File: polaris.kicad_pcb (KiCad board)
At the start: 4 copper layers, 75 x 155 mm, 163 parts, among them J1001 Conn_Coaxial, J101 XT60-M, J102 PYRO0, J103 PYRO1, J104 PYRO2, J105 PYRO3, J106 PYRO4, J107 PYRO5, J108 SERVO0, J109 SERVO1, J110 SERVO2, J111 SERVO3, J112 SERVO4, J113 SERVO5, J114 SPI, J115 I2C, J116 PB, J117 SWD, J301 USB_C_Receptacle_USB2.0_16P, J401 GNSS, J501 XT60-M, Q201 IRLZ44N, Q202 IRLZ44N, Q401 Q_NMOS, Q501 IRLZ44N, Q502 IRLZ44N, Q503 IRLZ44N, Q504 IRLZ44N, Q505 IRLZ44N, Q506 IRLZ44N, SW401 SW_Push, SW402 SW_Push, U1001 Ra-08H, U1101 THD-2528-11SD-GF, U1201 W25Q128JVE, U201 BQ24005, U202 LM74700, U203 LM74700, U204 TLV75733PDBV, U205 LMR51430, U206 TPS7A2033PDBVR, U301 USBLC6-2SC6, U302 CH224K, U303 USBLC6-2SC6, U403 STM32F446VETx, U501 PC817, U502 PC817, U503 PC817, U504 PC817, U505 PC817, U506 PC817, U507 CD4051B, U601 ICM-42688-P, U701 LSM6DSO32TR, U801 MS5607, U901 LPS22HH, Y401 YXC YSX321SL

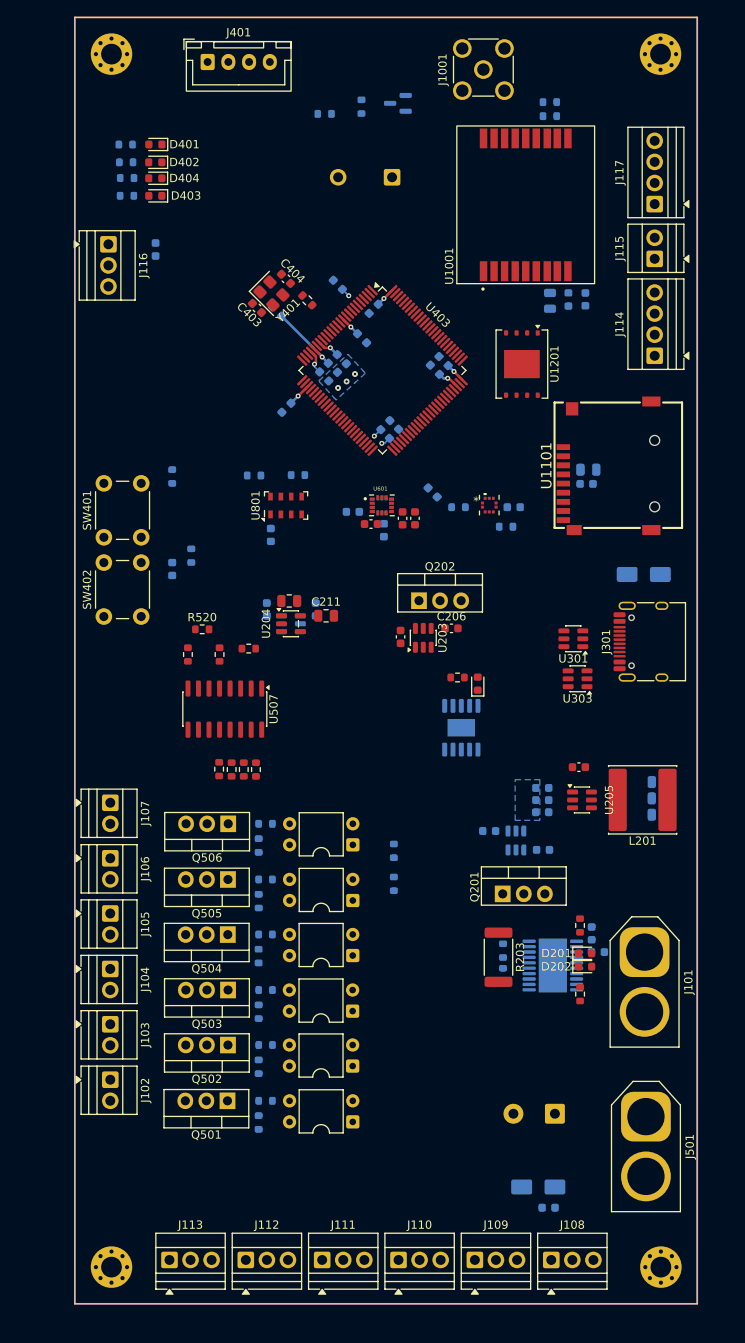
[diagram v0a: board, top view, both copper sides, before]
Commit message: Re-annotated schematic
Continued laying out traces on PCB
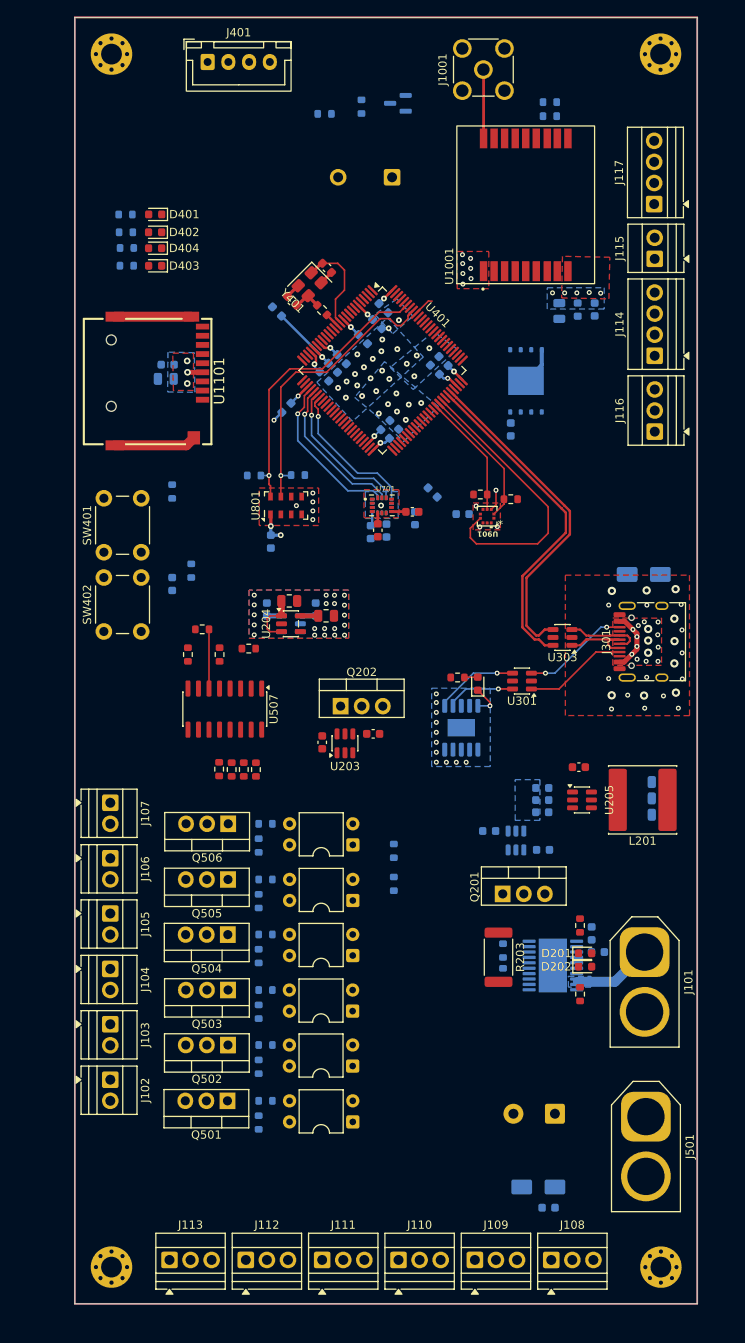
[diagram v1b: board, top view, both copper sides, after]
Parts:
- C601, C602, C603, U1201, U601: moved to B.Cu
- C701, C702, R901, R902, U701: moved to F.Cu
- moved J116 69.6 mm to (156.9, 74.9), turned to 90 degrees
- moved U1101 55.0 mm to (97.1, 68.8), turned to -90 degrees
- moved C1102 52.5 mm to (98.2, 66.8), turned to 180 degrees
- moved C1101 52.1 mm to (98.0, 68.6), turned to 180 degrees
- moved C1201 48.0 mm to (139.5, 74.6), turned to -90 degrees
- moved U203 15.8 mm to (119.5, 112.5)
- moved C206 15.8 mm to (123.0, 111.3)
- moved C204 15.8 mm to (116.8, 112.3)
- moved Q202 15.8 mm to (119.0, 108.0)
- moved C403 9.72 mm to (117.4, 55.2)
- moved D401 8.43 mm to (96.7, 48.7)
- moved D402 8.43 mm to (96.7, 50.9)
- moved D403 8.43 mm to (96.7, 54.9)
- moved D404 8.43 mm to (96.7, 52.8)
- moved R408 8.43 mm to (93.1, 48.7)
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- renumbered U403 to U401
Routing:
- net /2_USB/USB_D-: track 0.00 -> 40.6 mm
- net /2_USB/USB_D+: track 0.00 -> 40.2 mm
- net /3_NavigationProcessor/MS_SDA: track 0.00 -> 35.1 mm, vias 0 -> 1
- net /3_NavigationProcessor/MS_SCL: track 0.00 -> 34.8 mm, vias 0 -> 1
- net /3_NavigationProcessor/LPS_INT: track 0.00 -> 34.3 mm
- net GND: track 0.00 -> 31.3 mm, vias 3 -> 100
- net /3_NavigationProcessor/ICM_CS: track 0.00 -> 19.5 mm, vias 0 -> 1
- net /3_NavigationProcessor/ICM_SCK: track 0.00 -> 18.8 mm, vias 0 -> 1
- net /3_NavigationProcessor/ICM_MOSI: track 0.00 -> 17.8 mm, vias 0 -> 1
- net /3_NavigationProcessor/ICM_MISO: track 0.00 -> 17.7 mm, vias 0 -> 1
- net /3_NavigationProcessor/LPS_SCL: track 0.00 -> 17.0 mm
- net +3.3V: track 27.6 -> 43.0 mm, vias 9 -> 14
- net /3_NavigationProcessor/LPS_SDA: track 0.00 -> 14.9 mm
- net /2_USB/USBC_CC2: track 0.00 -> 12.9 mm, vias 0 -> 2
- net /2_USB/USBC_CC1: track 0.00 -> 12.5 mm
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- added copper zone on B.Cu, net +3.3V
- added copper zone on F.Cu, net +3.3V
- added copper zone on B.Cu, net +3.3VA
- added copper zone on F.Cu, net +3.3VA
- added copper zone on F.Cu, net /1_Power/USB_VCC
- added copper zone on F.Cu, net GND
- added copper zone on B.Cu, net VBAT_VIN
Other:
- board text added: "U901"

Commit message: Continued laying traces
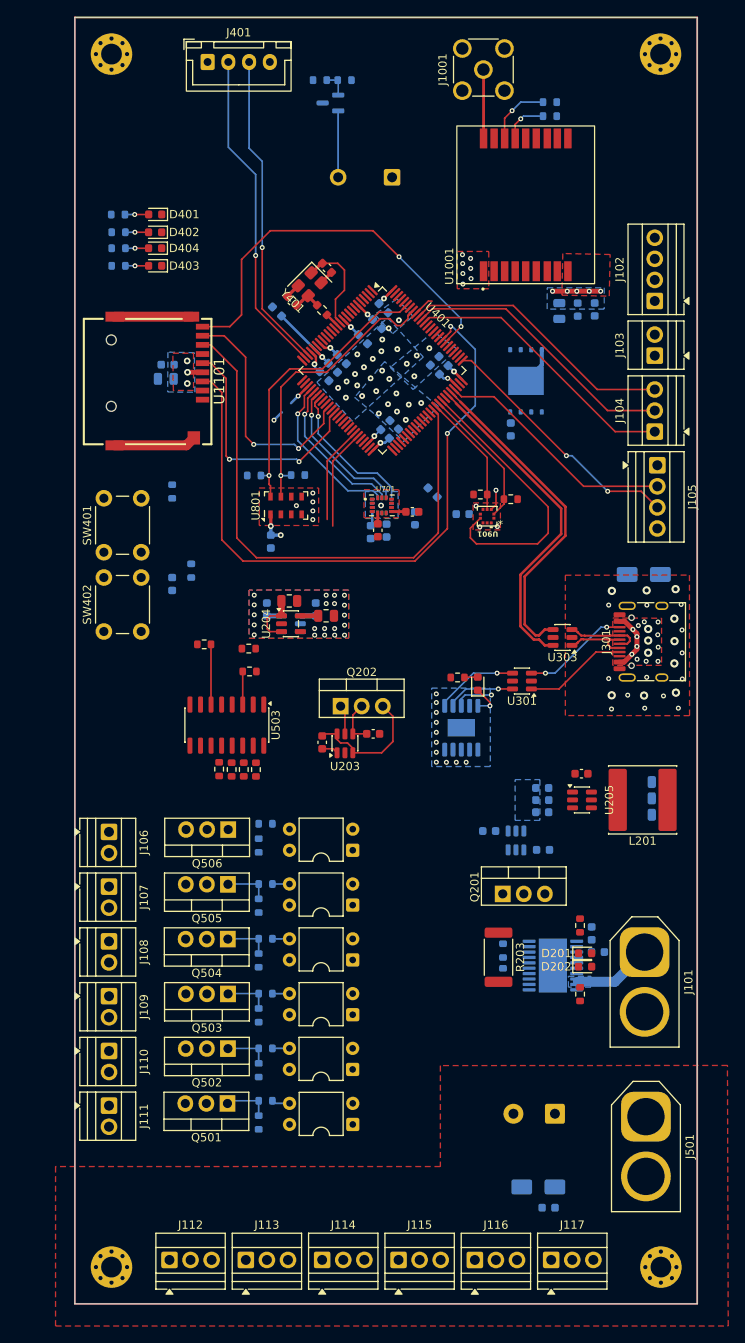
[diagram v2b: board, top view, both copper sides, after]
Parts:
- removed C417, C418, C419: 100n, Capacitor_SMD:C_0603_1608Metric
- removed R412, R413: 180R, Resistor_SMD:R_0603_1608Metric
- removed R414: 47R, Resistor_SMD:R_0603_1608Metric
- removed R415: 47k, Resistor_SMD:R_0603_1608Metric
- removed the R517 at (100.6, 101.8)
- removed the R518 at (104.4, 101.8)
- added C409: 100n, Capacitor_SMD:C_0603_1608Metric, B.Cu at (125.4, 75.2)
- added C412: 100n, Capacitor_SMD:C_0603_1608Metric, B.Cu at (117.1, 68.2)
- added R406: 47R, Resistor_SMD:R_0603_1608Metric, B.Cu at (119.5, 32.6)
- added R407: 47k, Resistor_SMD:R_0603_1608Metric, B.Cu at (116.5, 32.6)
- added R408: 180R, Resistor_SMD:R_0603_1608Metric, B.Cu at (92.3, 54.9)
- added R409: 180R, Resistor_SMD:R_0603_1608Metric, B.Cu at (92.3, 52.8)
- added R508: 1k, Resistor_SMD:R_0603_1608Metric, F.Cu at (108.1, 103.8)
- C406: renamed from C408; value 2u2 -> 4u7
- C410: value 4u7 -> 100n
- J102: value PYRO0 -> SPI; footprint TerminalBlock:TerminalBlock_Xinya_XY308-2.54-2P_1x02_P2.54mm_Horizontal -> TerminalBlock:TerminalBlock_Xinya_XY308-2.54-4P_1x04_P2.54mm_Horizontal
- J103: value PYRO1 -> I2C
- J104: value PYRO2 -> PB; footprint TerminalBlock:TerminalBlock_Xinya_XY308-2.54-2P_1x02_P2.54mm_Horizontal -> TerminalBlock:TerminalBlock_Xinya_XY308-2.54-3P_1x03_P2.54mm_Horizontal
- J105: value PYRO3 -> SWD; footprint TerminalBlock:TerminalBlock_Xinya_XY308-2.54-2P_1x02_P2.54mm_Horizontal -> TerminalBlock:TerminalBlock_Xinya_XY308-2.54-4P_1x04_P2.54mm_Horizontal
- J106: value PYRO4 -> PYRO5
- J107: value PYRO5 -> PYRO4
- J108: value SERVO0 -> PYRO3; footprint TerminalBlock:TerminalBlock_Xinya_XY308-2.54-3P_1x03_P2.54mm_Horizontal -> TerminalBlock:TerminalBlock_Xinya_XY308-2.54-2P_1x02_P2.54mm_Horizontal
- J109: value SERVO1 -> PYRO2; footprint TerminalBlock:TerminalBlock_Xinya_XY308-2.54-3P_1x03_P2.54mm_Horizontal -> TerminalBlock:TerminalBlock_Xinya_XY308-2.54-2P_1x02_P2.54mm_Horizontal
- J110: value SERVO2 -> PYRO1; footprint TerminalBlock:TerminalBlock_Xinya_XY308-2.54-3P_1x03_P2.54mm_Horizontal -> TerminalBlock:TerminalBlock_Xinya_XY308-2.54-2P_1x02_P2.54mm_Horizontal
- J111: value SERVO3 -> PYRO0; footprint TerminalBlock:TerminalBlock_Xinya_XY308-2.54-3P_1x03_P2.54mm_Horizontal -> TerminalBlock:TerminalBlock_Xinya_XY308-2.54-2P_1x02_P2.54mm_Horizontal
- J112: renamed from J113; value SERVO5 -> SERVO0
- J113: renamed from J112; value SERVO4 -> SERVO1
- J114: value SPI -> SERVO2; footprint TerminalBlock:TerminalBlock_Xinya_XY308-2.54-4P_1x04_P2.54mm_Horizontal -> TerminalBlock:TerminalBlock_Xinya_XY308-2.54-3P_1x03_P2.54mm_Horizontal
- J115: value I2C -> SERVO3; footprint TerminalBlock:TerminalBlock_Xinya_XY308-2.54-2P_1x02_P2.54mm_Horizontal -> TerminalBlock:TerminalBlock_Xinya_XY308-2.54-3P_1x03_P2.54mm_Horizontal
- J116: value PB -> SERVO4
- J117: value SWD -> SERVO5; footprint TerminalBlock:TerminalBlock_Xinya_XY308-2.54-4P_1x04_P2.54mm_Horizontal -> TerminalBlock:TerminalBlock_Xinya_XY308-2.54-3P_1x03_P2.54mm_Horizontal
- R517: renamed from R515; value 4k7 -> 47R
- R518: renamed from R516; value 4k7 -> 47R
- R519: value 1k -> 4k7
- U503: value PC817 -> CD4051B; footprint Package_DIP:DIP-4_W7.62mm -> Package_SO:SOIC-16_3.9x9.9mm_P1.27mm
- U507: value CD4051B -> PC817; footprint Package_SO:SOIC-16_3.9x9.9mm_P1.27mm -> Package_DIP:DIP-4_W7.62mm
- moved J117 127.8 mm to (144.4, 174.7), turned to 0 degrees
- moved J115 124.5 mm to (126.0, 174.7), turned to 0 degrees
- moved J114 116.1 mm to (116.8, 174.7), turned to 0 degrees
- moved J102 114.5 mm to (156.9, 59.2), turned to 90 degrees
- moved J103 103.9 mm to (156.9, 65.8), turned to 90 degrees
- moved J116 102.1 mm to (135.2, 174.7), turned to 0 degrees
- moved J104 92.2 mm to (156.9, 74.9), turned to 90 degrees
- moved J105 85.2 mm to (157.2, 79.0)
- moved J108 65.7 mm to (91.1, 136.3), turned to -90 degrees
- moved J109 54.3 mm to (91.1, 142.9), turned to -90 degrees
- moved J110 43.0 mm to (91.1, 149.5), turned to -90 degrees
- moved U503 37.6 mm to (105.3, 110.3), turned to -90 degrees
- moved J111 31.7 mm to (91.1, 156.1), turned to -90 degrees
- moved R207 28.2 mm to (152.4, 116.9)
- moved R206 28.2 mm to (152.4, 121.1)
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- renumbered C403 to C401, C404 to C402, C405 to C403, C406 to C404, C407 to C405, C409 to C407, R405 to R401, R406 to R402, R407 to R403, R408 to R404, R409 to R405, R520 to R507, R507 to R509, R508 to R510, R509 to R511, R510 to R512, R511 to R513, R512 to R514, R513 to R515, R514 to R516
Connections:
- C406 pad 1: Net-(U403-VCAP_1) -> +3.3V
- J102 pad 1: POWER -> /3_NavigationProcessor/SPI4_SCK
- J102 pad 2: /4_Pyrochannels/PYRO_0 -> /3_NavigationProcessor/SPI4_NSS
- J103 pad 1: POWER -> /3_NavigationProcessor/I2C2_SCL
- J103 pad 2: /4_Pyrochannels/PYRO_1 -> /3_NavigationProcessor/I2C2_SDA
- J104 pad 1: POWER -> /3_NavigationProcessor/PB3
- J104 pad 2: /4_Pyrochannels/PYRO_2 -> /3_NavigationProcessor/PB4
- J105 pad 1: POWER -> +3.3V
- J105 pad 2: /4_Pyrochannels/PYRO_3 -> /3_NavigationProcessor/SYS_SWDIO
- J106 pad 2: /4_Pyrochannels/PYRO_4 -> /4_Pyrochannels/PYRO_5
- J107 pad 2: /4_Pyrochannels/PYRO_5 -> /4_Pyrochannels/PYRO_4
- J108 pad 1: /3_NavigationProcessor/SERVO_S0 -> POWER
- J108 pad 2: /4_Pyrochannels/SERVO_PWR -> /4_Pyrochannels/PYRO_3
- J109 pad 1: /3_NavigationProcessor/SERVO_S1 -> POWER
- J109 pad 2: /4_Pyrochannels/SERVO_PWR -> /4_Pyrochannels/PYRO_2
- J110 pad 1: /3_NavigationProcessor/SERVO_S2 -> POWER
- J110 pad 2: /4_Pyrochannels/SERVO_PWR -> /4_Pyrochannels/PYRO_1
- J111 pad 1: /3_NavigationProcessor/SERVO_S3 -> POWER
- J111 pad 2: /4_Pyrochannels/SERVO_PWR -> /4_Pyrochannels/PYRO_0
- J112 pad 1: /3_NavigationProcessor/SERVO_S5 -> /3_NavigationProcessor/SERVO_S0
- J113 pad 1: /3_NavigationProcessor/SERVO_S4 -> /3_NavigationProcessor/SERVO_S1
- J114 pad 1: /3_NavigationProcessor/SPI4_SCK -> /3_NavigationProcessor/SERVO_S2
- J114 pad 2: /3_NavigationProcessor/SPI4_NSS -> /4_Pyrochannels/SERVO_PWR
- J114 pad 3: /3_NavigationProcessor/SPI4_MISO -> GND
- J115 pad 1: /3_NavigationProcessor/I2C2_SCL -> /3_NavigationProcessor/SERVO_S3
- J115 pad 2: /3_NavigationProcessor/I2C2_SDA -> /4_Pyrochannels/SERVO_PWR
- J116 pad 1: /3_NavigationProcessor/PB3 -> /3_NavigationProcessor/SERVO_S4
- J116 pad 2: /3_NavigationProcessor/PB4 -> /4_Pyrochannels/SERVO_PWR
- J116 pad 3: /3_NavigationProcessor/PB5 -> GND
- J117 pad 1: +3.3V -> /3_NavigationProcessor/SERVO_S5
- J117 pad 2: /3_NavigationProcessor/SYS_SWDIO -> /4_Pyrochannels/SERVO_PWR
- J117 pad 3: /3_NavigationProcessor/SYS_SWCLK -> GND
- Q501 pad 2: GND -> /4_Pyrochannels/PYRO_0
- Q501 pad 3: /4_Pyrochannels/PYRO_0 -> GND
- Q502 pad 2: GND -> /4_Pyrochannels/PYRO_1
- Q502 pad 3: /4_Pyrochannels/PYRO_1 -> GND
- Q503 pad 2: GND -> /4_Pyrochannels/PYRO_2
- Q503 pad 3: /4_Pyrochannels/PYRO_2 -> GND
- Q504 pad 2: GND -> /4_Pyrochannels/PYRO_3
- Q504 pad 3: /4_Pyrochannels/PYRO_3 -> GND
- Q505 pad 2: GND -> /4_Pyrochannels/PYRO_4
- Q505 pad 3: /4_Pyrochannels/PYRO_4 -> GND
- Q506 pad 2: GND -> /4_Pyrochannels/PYRO_5
- Q506 pad 3: /4_Pyrochannels/PYRO_5 -> GND
- R507 pad 1: +3.3V -> /4_Pyrochannels/PYRO_5
- R507 pad 2: /3_NavigationProcessor/~{MUX_EN} -> /4_Pyrochannels/PYRO_5
- R509 pad 2: Net-(R507-Pad2) -> Net-(R509-Pad2)
- R510 pad 2: Net-(R508-Pad2) -> Net-(R510-Pad2)
- R515 pad 2: Net-(R513-Pad2) -> Net-(R515-Pad2)
- R516 pad 2: Net-(R514-Pad2) -> Net-(R516-Pad2)
- R517 pad 2: GND -> Net-(R515-Pad2)
- R518 pad 2: GND -> Net-(R516-Pad2)
- R519 pad 1: /3_NavigationProcessor/PYRO_SENSE -> /4_Pyrochannels/PYRO_4
- R519 pad 2: GND -> /4_Pyrochannels/PYRO_4
- U401 pad 48: Net-(U403-VCAP_1) -> Net-(U401-VCAP_1)
- U503 pad 1: /3_NavigationProcessor/PYRO_2 -> /4_Pyrochannels/PYRO_4
- U503 pad 2: GND -> unconnected-(U503-X6-Pad2)
- U503 pad 3: Net-(R507-Pad2) -> /3_NavigationProcessor/PYRO_SENSE
- U503 pad 4: +5V -> unconnected-(U503-X7-Pad4)
- U504 pad 1: /3_NavigationProcessor/PYRO_3 -> /3_NavigationProcessor/PYRO_2
- U504 pad 3: Net-(R508-Pad2) -> Net-(R509-Pad2)
- U505 pad 1: /3_NavigationProcessor/PYRO_4 -> /3_NavigationProcessor/PYRO_3
- U505 pad 3: Net-(R513-Pad2) -> Net-(R510-Pad2)
- U506 pad 1: /3_NavigationProcessor/PYRO_5 -> /3_NavigationProcessor/PYRO_4
- U506 pad 3: Net-(R514-Pad2) -> Net-(R515-Pad2)
- U507 pad 1: /4_Pyrochannels/PYRO_4 -> /3_NavigationProcessor/PYRO_5
- U507 pad 2: unconnected-(U507-X6-Pad2) -> GND
- U507 pad 3: /3_NavigationProcessor/PYRO_SENSE -> Net-(R516-Pad2)
- U507 pad 4: unconnected-(U507-X7-Pad4) -> +5V
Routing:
- net /3_NavigationProcessor/SD_CMD: track 0.00 -> 79.7 mm, vias 0 -> 2
- net /3_NavigationProcessor/SD_DAT0: track 0.00 -> 67.2 mm
- net /3_NavigationProcessor/SD_CD: track 0.00 -> 48.0 mm, vias 0 -> 2
- net /3_NavigationProcessor/GPS_TX: track 0.00 -> 39.5 mm, vias 0 -> 1
- net /3_NavigationProcessor/GPS_RX: track 0.00 -> 38.2 mm, vias 0 -> 1
- net /3_NavigationProcessor/PB4: track 0.00 -> 33.7 mm
- net /3_NavigationProcessor/PB3: track 0.00 -> 33.7 mm
- net /3_NavigationProcessor/PB5: track 0.00 -> 33.2 mm
- net /3_NavigationProcessor/SYS_SWCLK: track 0.00 -> 30.8 mm, vias 0 -> 2
- net /3_NavigationProcessor/SD_CLK: track 0.00 -> 29.7 mm, vias 0 -> 2
- net /3_NavigationProcessor/SYS_SWDIO: track 0.00 -> 29.4 mm
- net /3_NavigationProcessor/SD_DAT1: track 0.00 -> 29.3 mm, vias 0 -> 2
- net /1_Power/USB_VCC: track 7.32 -> 27.6 mm, vias 15 -> 16
- net /3_NavigationProcessor/SERVO_S5: track 0.00 -> 12.1 mm
- net /3_NavigationProcessor/SERVO_S4: track 0.00 -> 11.8 mm
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- added copper zone on F.Cu, net /4_Pyrochannels/SERVO_PWR
- added copper zone on In2.Cu, net POWER

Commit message: Continued laying traces on PCB
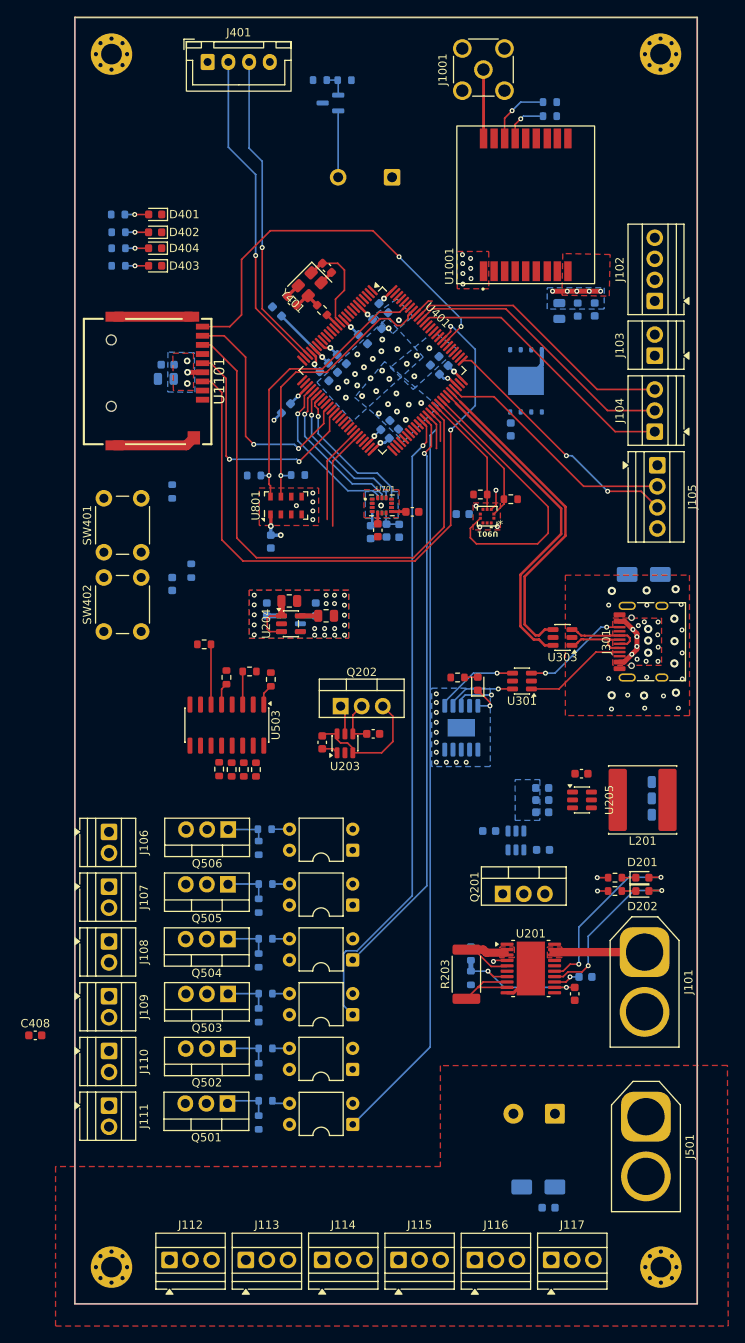
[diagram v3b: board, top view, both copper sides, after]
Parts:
- added C408: 4u7, Capacitor_SMD:C_0603_1608Metric, F.Cu at (82.2, 147.7)
- added R520: 4k7, Resistor_SMD:R_0603_1608Metric, F.Cu at (105.3, 104.5)
- C201, U201: moved to F.Cu
- C406: value 4u7 -> 2u2
- R517, R518: value 47R -> 4k7
- moved C410 20.4 mm to (112.4, 72.1), turned to -135 degrees
- moved R205 13.1 mm to (152.1, 130.3), turned to 180 degrees
- moved D201 11.4 mm to (155.4, 128.7)
- moved D202 11.4 mm to (155.4, 130.3)
- moved C201 7.57 mm to (147.2, 142.7), turned to -90 degrees
- moved R204 7.14 mm to (152.1, 128.7), turned to 180 degrees
- moved R519 4.57 mm to (110.6, 104.8), turned to 90 degrees
- moved R203 4.38 mm to (134.2, 140.3), turned to 90 degrees
- moved R202 3.88 mm to (134.7, 140.7)
- moved R201 3.88 mm to (134.7, 137.8)
- moved C202 3.35 mm to (148.5, 140.6)
- moved U201 2.68 mm to (141.9, 139.6)
- moved C601 2.43 mm to (126.1, 86.9)
- moved R516 0.66 mm to (109.9, 122.8), turned to 0 degrees
- moved R518 0.29 mm to (109.2, 125.1)
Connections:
- net /1_Power/VSENSE renamed /1_Power/IN
- C406 pad 1: +3.3V -> Net-(U401-VCAP_1)
- R507 pad 1: /4_Pyrochannels/PYRO_5 -> +3.3V
- R507 pad 2: /4_Pyrochannels/PYRO_5 -> /3_NavigationProcessor/~{MUX_EN}
- R517 pad 2: Net-(R515-Pad2) -> GND
- R518 pad 2: Net-(R516-Pad2) -> GND
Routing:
- net /3_NavigationProcessor/PYRO_0: track 0.00 -> 92.4 mm
- net /3_NavigationProcessor/PYRO_2: track 0.00 -> 77.1 mm, vias 0 -> 1
- net /3_NavigationProcessor/PYRO_3: track 0.00 -> 69.8 mm, vias 0 -> 1
- net /1_Power/CHG_STAT2: track 0.00 -> 21.6 mm, vias 0 -> 2
- net /1_Power/CHG_STAT1: track 0.00 -> 20.9 mm, vias 0 -> 2
- net /1_Power/BATT_APG: track 0.00 -> 18.6 mm, vias 0 -> 2
- net /1_Power/IN: track 0.00 -> 11.5 mm
- net /1_Power/USB_VCC: track 27.6 -> 38.5 mm, vias 16 -> 17
- net /3_NavigationProcessor/~{MUX_EN}: track 0.00 -> 7.14 mm
- net Net-(Q506-G): track 0.00 -> 5.07 mm
- net GND: track 31.3 -> 35.8 mm
- net /4_Pyrochannels/PYRO_5: track 7.14 -> 2.69 mm
- net /3_NavigationProcessor/PYRO_1: track 0.00 -> 3.96 mm
- net Net-(U201-TMR_SEL): track 0.00 -> 3.27 mm, vias 0 -> 1
- net +3.3V: track 45.6 -> 48.5 mm, vias 15 -> 16
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- added copper zone on F.Cu, net /1_Power/IN
- added copper zone on F.Cu, net VBAT_VIN
- removed copper zone on B.Cu, net VBAT_VIN
